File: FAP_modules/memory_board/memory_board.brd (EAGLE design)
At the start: 100 x 60 mm, 29 parts, among them IC1 74HC32, IC2 74HC04, IC4 74HC245DW, IC5 AT28C256

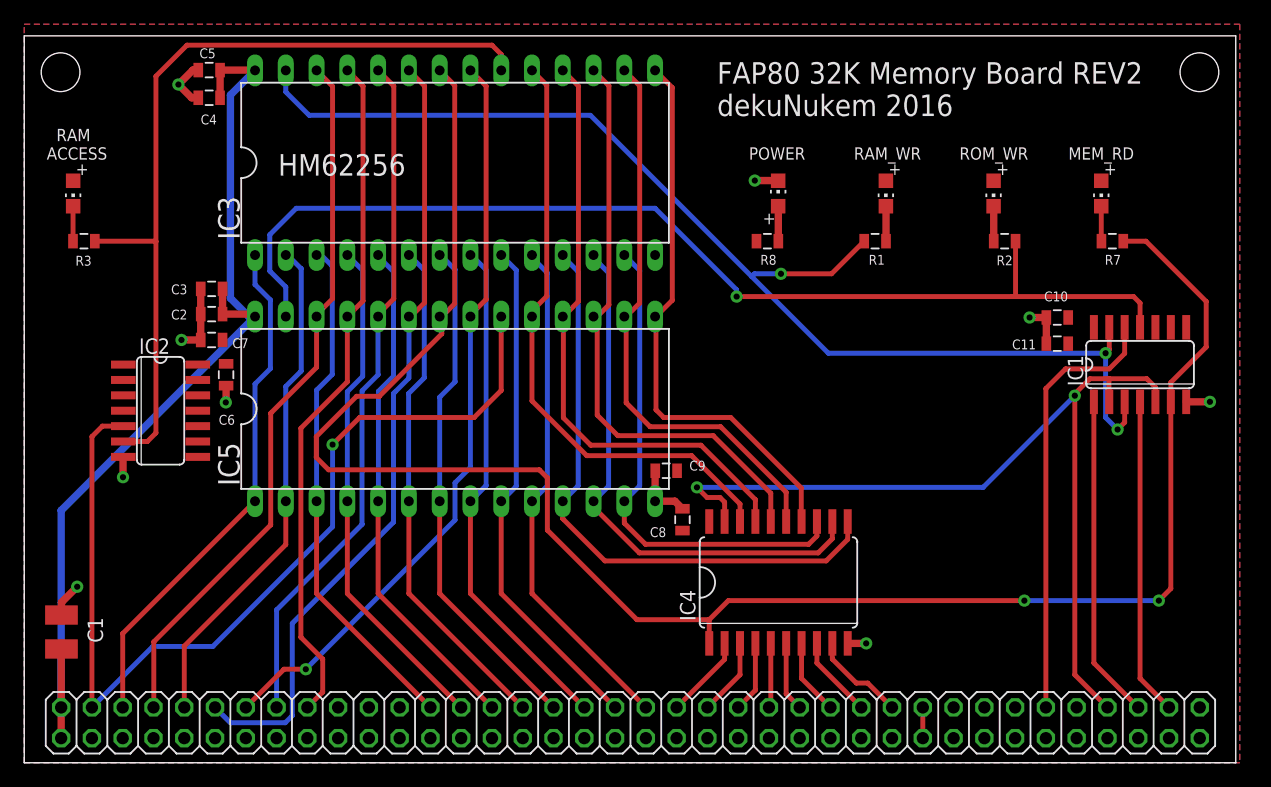
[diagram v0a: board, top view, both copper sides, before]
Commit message: new memory board
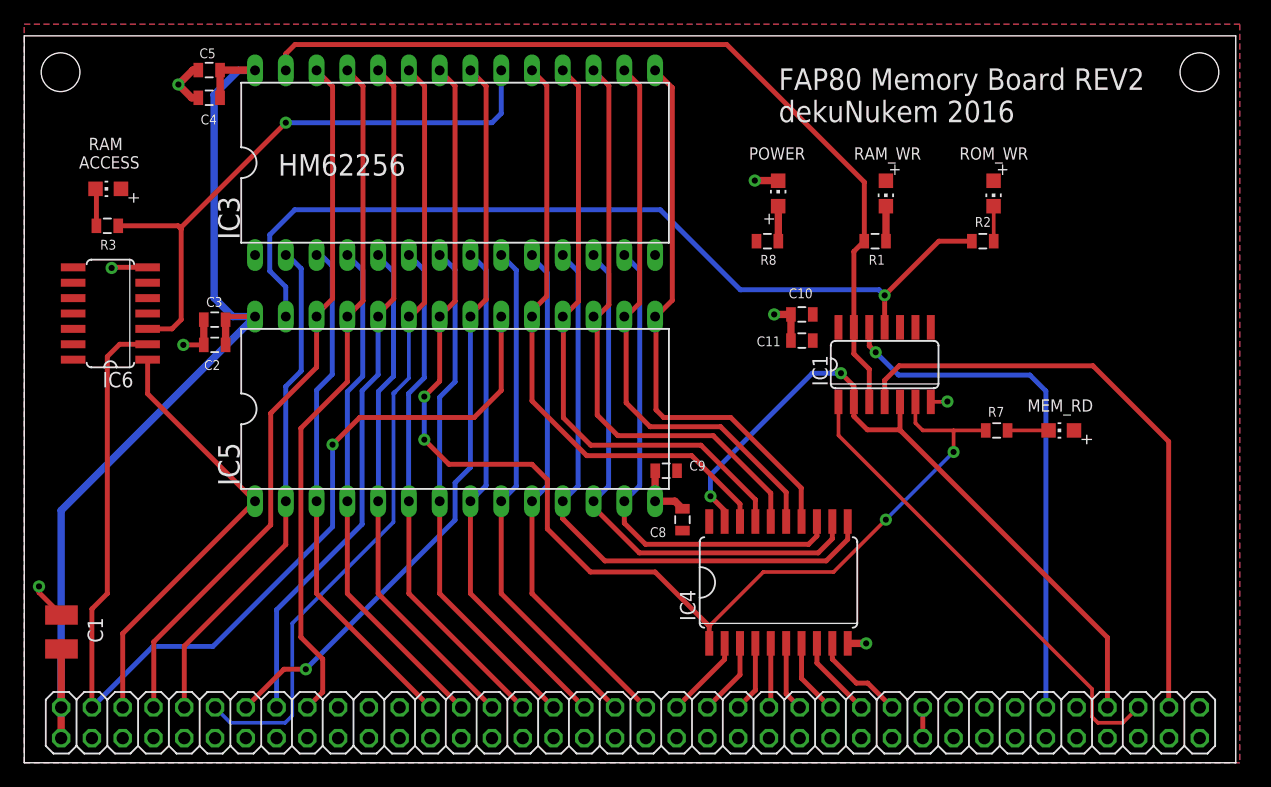
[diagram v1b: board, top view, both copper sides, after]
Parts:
- removed C6: 10nF, SparkFun-Capacitors:0805
- removed C7: 100nF, SparkFun-Capacitors:0805
- removed IC2: 74HC04, 74xx-us:SO14
- added IC6: 74HC00D, 74xx-eu:SO14
- R1, R2, R3, R7, R8: value 50 -> 2K
- moved C10 21.1 mm to (64.2, 37.0)
- moved C11 21.1 mm to (64.2, 34.8)
- moved IC1 21.1 mm to (71.0, 32.9)
- moved LED2 19.8 mm to (85.6, 27.4), turned to 90 degrees
- moved R7 18.3 mm to (80.3, 27.4), turned to 0 degrees
- moved LED5 2.92 mm to (6.93, 47.4), turned to 90 degrees
- moved C2 2.55 mm to (15.7, 34.5)
- moved C3 2.55 mm to (15.7, 36.6)
- moved R3 2.31 mm to (6.86, 44.3)
- moved R2 1.80 mm to (79.1, 43.1), turned to 0 degrees
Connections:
- net +3V3: now also IC1.10, IC1.9, IC3.1, IC6.10, IC6.12, IC6.13, IC6.14, IC6.4, IC6.5, IC6.9; no longer C6.1, C7.1, IC2.1, IC2.11, IC2.13, IC2.14, IC2.3, IC2.9
- net GND: now also IC6.7; no longer C6.2, C7.2, IC2.7
- net N$32: now also IC6.2; no longer IC2.5
- net N$9: now also IC6.1; no longer IC3.1
- net RAM_ACCESS: now also IC6.3; no longer IC2.6
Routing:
- net MEM_RD: track 153.9 -> 101.5 mm, vias 2 -> 4
- net RAM_WR: track 100.4 -> 73.2 mm, vias 3 -> 0
- net RD: track 26.2 -> 50.3 mm
- net RAM_ACCESS: track 68.7 -> 49.9 mm, vias 0 -> 1
- net MREQ: track 76.3 -> 59.2 mm
- net EEP_WR: track 90.2 -> 73.5 mm
- net WR: track 26.7 -> 39.2 mm
- net N$32: track 80.0 -> 87.9 mm
- net BUSACK: track 36.2 -> 43.8 mm, vias 0 -> 1
- net N$9: track 42.9 -> 36.9 mm
- net +5V: track 78.6 -> 81.6 mm
- net GND: track 30.0 -> 27.6 mm, vias 9 -> 8
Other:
- board text added: "FAP80 Memory Board REV2 dekuNukem 2016"
- board text removed: "FAP80 32K Memory Board REV2 dekuNukem 2016"
